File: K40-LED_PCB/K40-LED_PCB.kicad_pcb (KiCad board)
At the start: 2 copper layers, 41 x 27.8 mm, 14 parts, among them p1 12V_Pad

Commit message: Trace  deletion
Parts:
- D1, D10, D11, D12, D2, D3, D4, D5, D6, D7, D8, D9: footprint LRST-C190KGKT:LEDC1608X35N -> SPMWH1228FD5WATUS3_FOOTPRINT:LED_SPMWH1228FD5WARMSE
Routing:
- net Net-(D1-PadA): track 50.5 -> 0.00 mm
- net Net-(D10-PadC): track 33.1 -> 0.00 mm
- net Net-(R1-Pad1): track 7.19 -> 0.00 mm
- net Net-(D5-PadC): track 5.64 -> 0.00 mm
- net Net-(D3-PadC): track 5.64 -> 0.00 mm
- net Net-(D10-PadA): track 5.64 -> 0.00 mm
- net Net-(D11-PadA): track 5.62 -> 0.00 mm
- net Net-(D6-PadC): track 5.62 -> 0.00 mm
- net Net-(D1-PadC): track 5.62 -> 0.00 mm
- net Net-(D2-PadC): track 4.97 -> 0.00 mm
- net Net-(D12-PadA): track 4.89 -> 0.00 mm
- net Net-(D4-PadC): track 4.89 -> 0.00 mm

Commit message: More Footprint updates
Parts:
- R1: value 200 -> 18
- p1: footprint 12V_Pad:12V_Supply_Pad -> 12V_Through_Hole:12V_Through_Hole
- moved p1 15.7 mm to (92.0, 77.0), turned to 90 degrees
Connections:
- D10 pad A: Net-(D10-PadA) -> Net-(D1-PadA)
- D11 pad A: Net-(D11-PadA) -> Net-(D10-PadC)
- D11 pad C: Net-(D10-PadC) -> Net-(D11-PadC)
- D12 pad A: Net-(D12-PadA) -> Net-(D11-PadC)
- D12 pad C: Net-(D10-PadC) -> Net-(D12-PadC)
- D7 pad C: Net-(D10-PadA) -> Net-(D12-PadC)
- D8 pad C: Net-(D11-PadA) -> Net-(D12-PadC)
- D9 pad C: Net-(D12-PadA) -> Net-(D12-PadC)
- p1 pad 1: Net-(R1-Pad1) -> Net-(D12-PadC)
- p1 pad 2: Net-(D10-PadC) -> Net-(R1-Pad1)

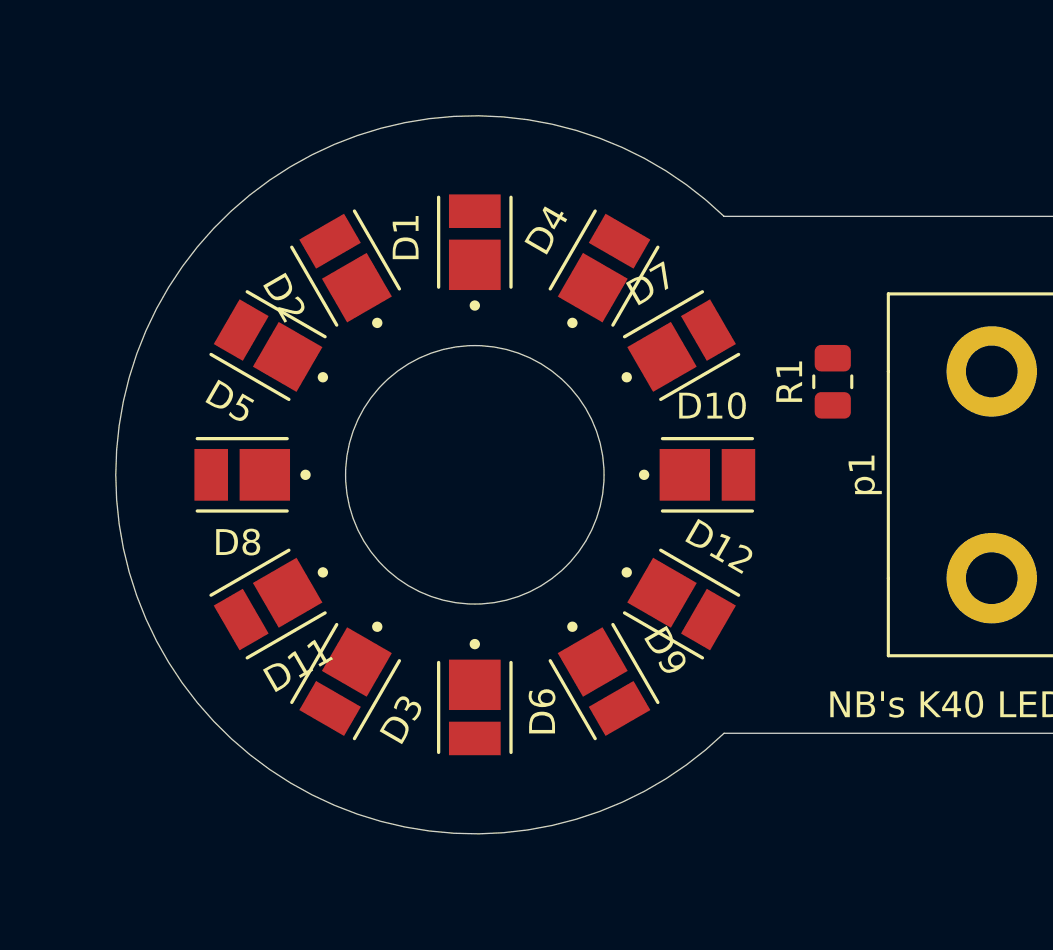
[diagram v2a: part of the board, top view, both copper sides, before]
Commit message: removed old footprint associations
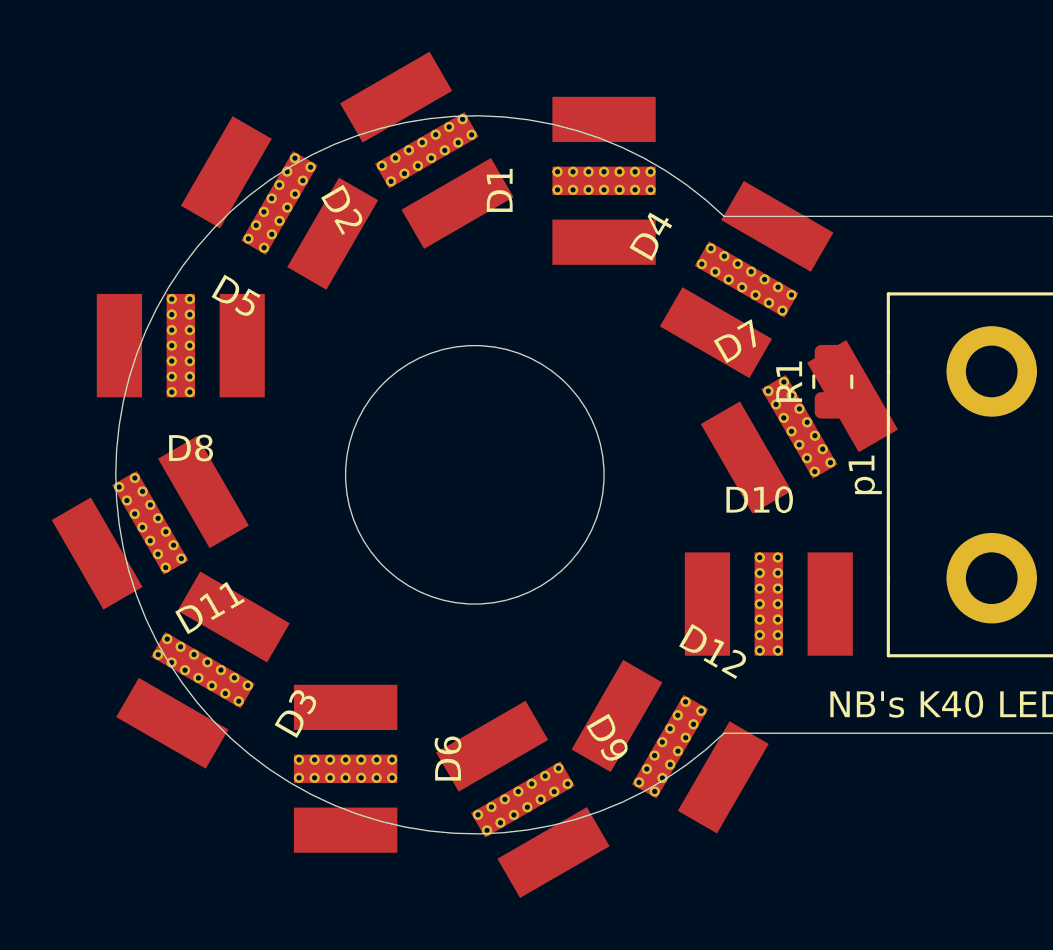
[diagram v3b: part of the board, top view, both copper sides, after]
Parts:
- D1, D10, D11, D12, D2, D3, D4, D5, D6, D7, D8, D9: footprint SPMWH1228FD5WATUS3_FOOTPRINT:LED_SPMWH1228FD5WARMSE -> Cree_MX3AWT-A1-R250-000BE3:Cree_MX3AWT-A1-R250-000BE3

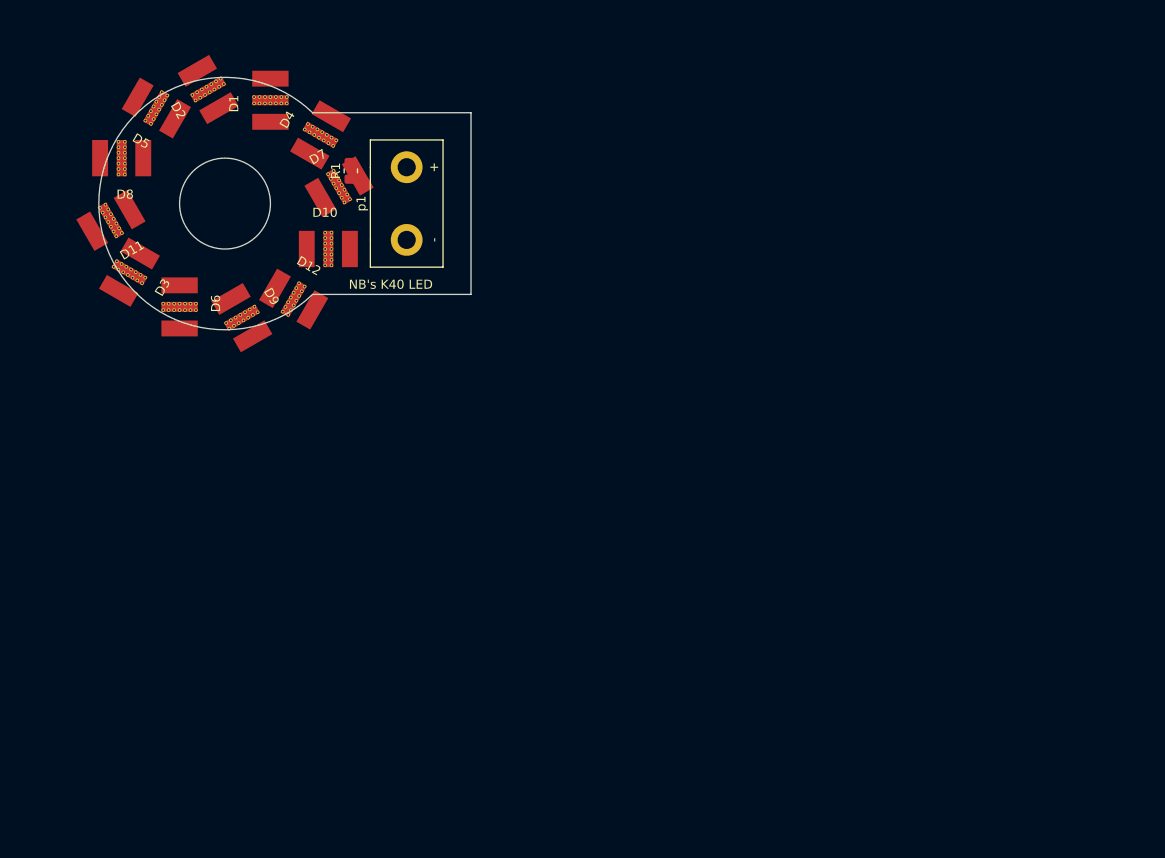
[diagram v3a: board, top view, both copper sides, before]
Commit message: PCB_Changes  + footprints
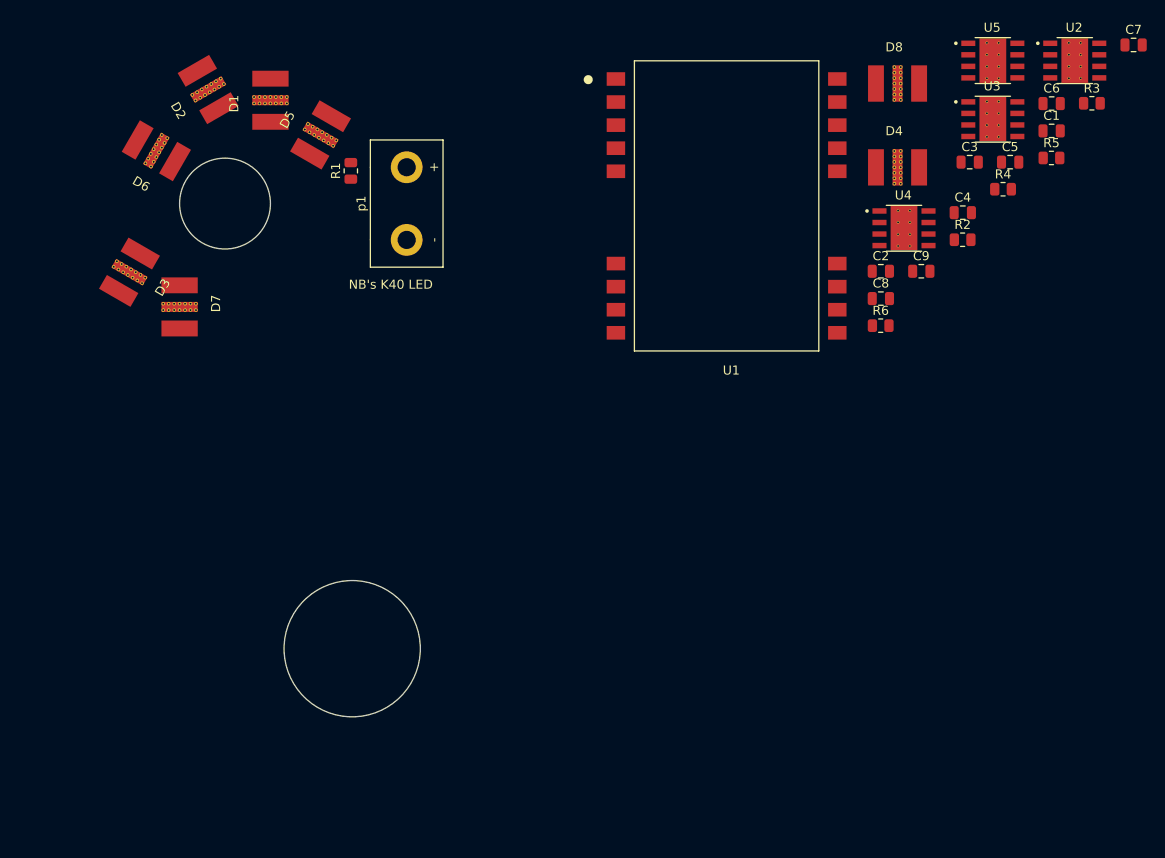
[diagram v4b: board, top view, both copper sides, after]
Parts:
- removed D10, D11, D12, D9: LTST-C190KGKT, Cree_MX3AWT-A1-R250-000BE3:Cree_MX3AWT-A1-R250-000BE3
- removed the D7 at (85.0, 68.0)
- added C1: 0.01uF, Capacitor_SMD:C_0805_2012Metric, F.Cu at (168.0, 65.0)
- added C2: 1uF, Capacitor_SMD:C_0805_2012Metric, F.Cu at (149.2, 80.5)
- added C3: 0.01uF, Capacitor_SMD:C_0805_2012Metric, F.Cu at (159.0, 68.4)
- added C4: 1uF, Capacitor_SMD:C_0805_2012Metric, F.Cu at (158.2, 74.0)
- added C5: 0.01uF, Capacitor_SMD:C_0805_2012Metric, F.Cu at (163.4, 68.4)
- added C6: 1uF, Capacitor_SMD:C_0805_2012Metric, F.Cu at (168.0, 62.0)
- added C7: 0.01uF, Capacitor_SMD:C_0805_2012Metric, F.Cu at (177.0, 55.5)
- added C8: 1uF, Capacitor_SMD:C_0805_2012Metric, F.Cu at (149.2, 83.5)
- added C9: 1uF, Capacitor_SMD:C_0805_2012Metric, F.Cu at (153.7, 80.5)
- added D4: LTST-C190KGKT, Cree_MX3AWT-A1-R250-000BE3:Cree_MX3AWT-A1-R250-000BE3, F.Cu at (148.7, 64.0)
- added R2: 1, Resistor_SMD:R_0805_2012Metric, F.Cu at (158.2, 77.0)
- added R3: 1, Resistor_SMD:R_0805_2012Metric, F.Cu at (172.4, 62.0)
- added R4: 1, Resistor_SMD:R_0805_2012Metric, F.Cu at (162.7, 71.4)
- added R5: 1, Resistor_SMD:R_0805_2012Metric, F.Cu at (168.0, 68.0)
- added R6: 51.1, Resistor_SMD:R_0805_2012Metric, F.Cu at (149.2, 86.4)
- added U1: LDD_350HS, LDD-350HS:LDD-350HS, F.Cu at (120.0, 54.8)
- added U2: LM3466, LM3466:NOPB, F.Cu at (170.5, 57.3)
- added U3: LM3466, LM3466:NOPB, F.Cu at (161.5, 63.7)
- added U4: LM3466, LM3466:NOPB, F.Cu at (151.7, 75.7)
- added U5: LM3466, LM3466:NOPB, F.Cu at (161.5, 57.3)
- R1: value 18 -> 13
- moved D8 82.7 mm to (148.7, 54.8), turned to 0 degrees
- moved D6 4.71 mm to (69.0, 72.7)
- renumbered D4 to D5, D5 to D6, D6 to D7
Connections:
- D1 pad A: Net-(D1-PadA) -> Net-(C1-Pad1)
- D2 pad A: Net-(D1-PadA) -> Net-(C1-Pad1)
- D3 pad A: Net-(D1-PadA) -> Net-(C1-Pad1)
- D6 pad C: Net-(D5-PadC) -> Net-(C4-Pad1)
- D8 pad A: Net-(D5-PadC) -> Net-(D4-PadC)
- D8 pad C: Net-(D12-PadC) -> Net-(C8-Pad1)
- R1 pad 2: Net-(D1-PadA) -> Net-(R1-Pad2)
- p1 pad 1: Net-(D12-PadC) -> Net-(p1-Pad1)
- p1 pad 2: Net-(R1-Pad1) -> Net-(p1-Pad2)
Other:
- board size 41 x 27.8 mm -> 26.5 x 61.5 mm

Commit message: PCB_Updates
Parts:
- moved D4 75.5 mm to (107.0, 127.0), turned to 180 degrees
- moved D8 71.8 mm to (106.9, 113.2), turned to 225 degrees
- moved D7 60.4 mm to (99.8, 137.9), turned to 135 degrees
- moved D3 58.7 mm to (85.9, 138.0), turned to 90 degrees
- moved D6 58.3 mm to (74.6, 130.7), turned to 45 degrees
- moved D2 52.0 mm to (74.6, 117.0), turned to 0 degrees
- moved D1 46.3 mm to (96.0, 106.2), turned to 270 degrees
- moved D5 41.7 mm to (82.2, 106.7), turned to 315 degrees

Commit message: PCB_Circular_Formation
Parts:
- moved D8 1.15 mm to (105.9, 113.7)
- moved D5 1.08 mm to (83.2, 107.1)
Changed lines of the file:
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@@
   )
   (module Cree_MX3AWT-A1-R250-000BE3:Cree_MX3AWT-A1-R250-000BE3 (layer F.Cu)
-    (at 106.894291 113.176777 225)
+    (at 105.894291 113.744134 225)
     (fp_text reference D8 (at 2 1 45) (layer F.SilkS)
       (effects (font (size 1 1) (thickness 0.15)))
@@
   )
   (module Cree_MX3AWT-A1-R250-000BE3:Cree_MX3AWT-A1-R250-000BE3 (layer F.Cu)
-    (at 82.176777 106.705127 315)
+    (at 83.176777 107.105709 315)
     (fp_text reference D5 (at 2 1 135) (layer F.SilkS)
       (effects (font (size 1 1) (thickness 0.15)))

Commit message: More circular changes correct
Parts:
- moved D6 1.73 mm to (76.1, 129.8)
- moved D7 1.41 mm to (98.8, 136.9)
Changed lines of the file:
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@@
   )
   (module Cree_MX3AWT-A1-R250-000BE3:Cree_MX3AWT-A1-R250-000BE3 (layer F.Cu)
-    (at 99.823223 137.894291 135)
+    (at 98.823223 136.894291 135)
     (fp_text reference D7 (at 2 1 135) (layer F.SilkS)
       (effects (font (size 1 1) (thickness 0.15)))
@@
   )
   (module Cree_MX3AWT-A1-R250-000BE3:Cree_MX3AWT-A1-R250-000BE3 (layer F.Cu)
-    (at 74.613621 130.705127 45)
+    (at 76.105709 129.823223 45)
     (fp_text reference D6 (at 2 1 45) (layer F.SilkS)
       (effects (font (size 1 1) (thickness 0.15)))

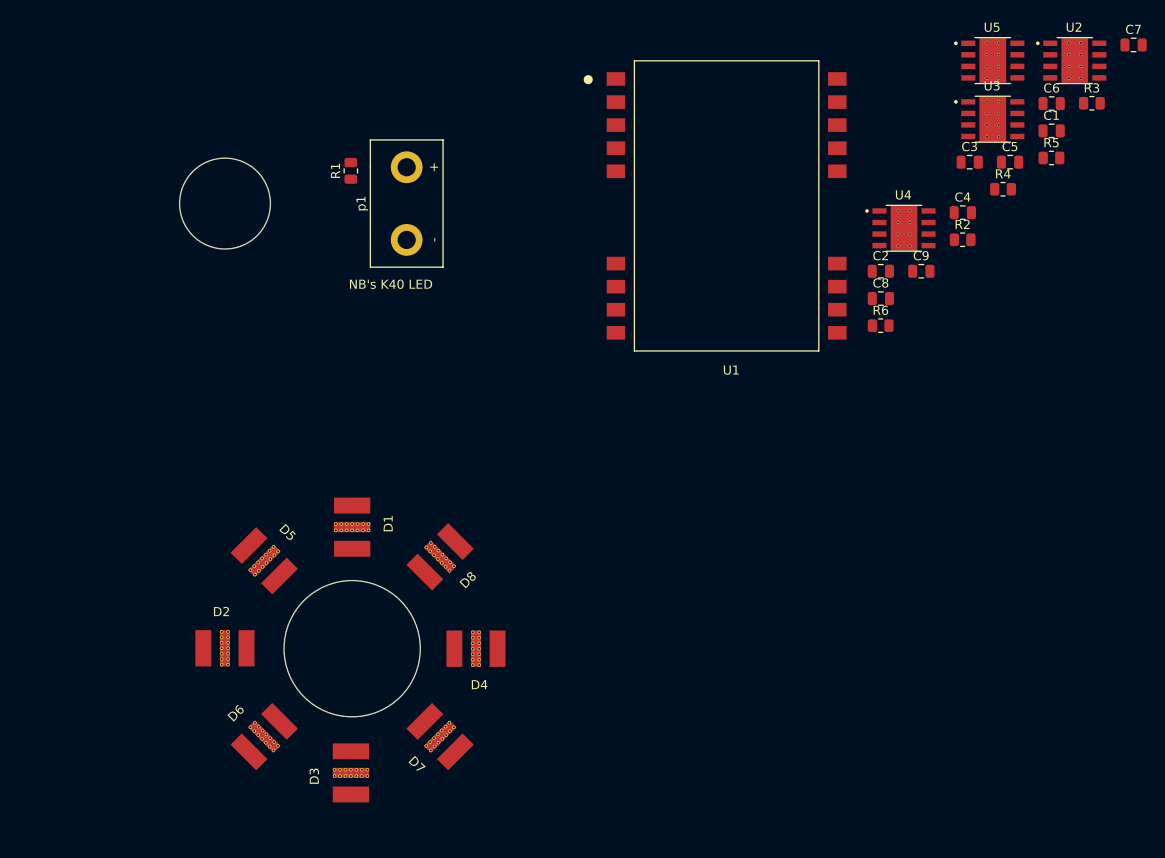
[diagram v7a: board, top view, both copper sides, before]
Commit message: PCB  Cathode traces
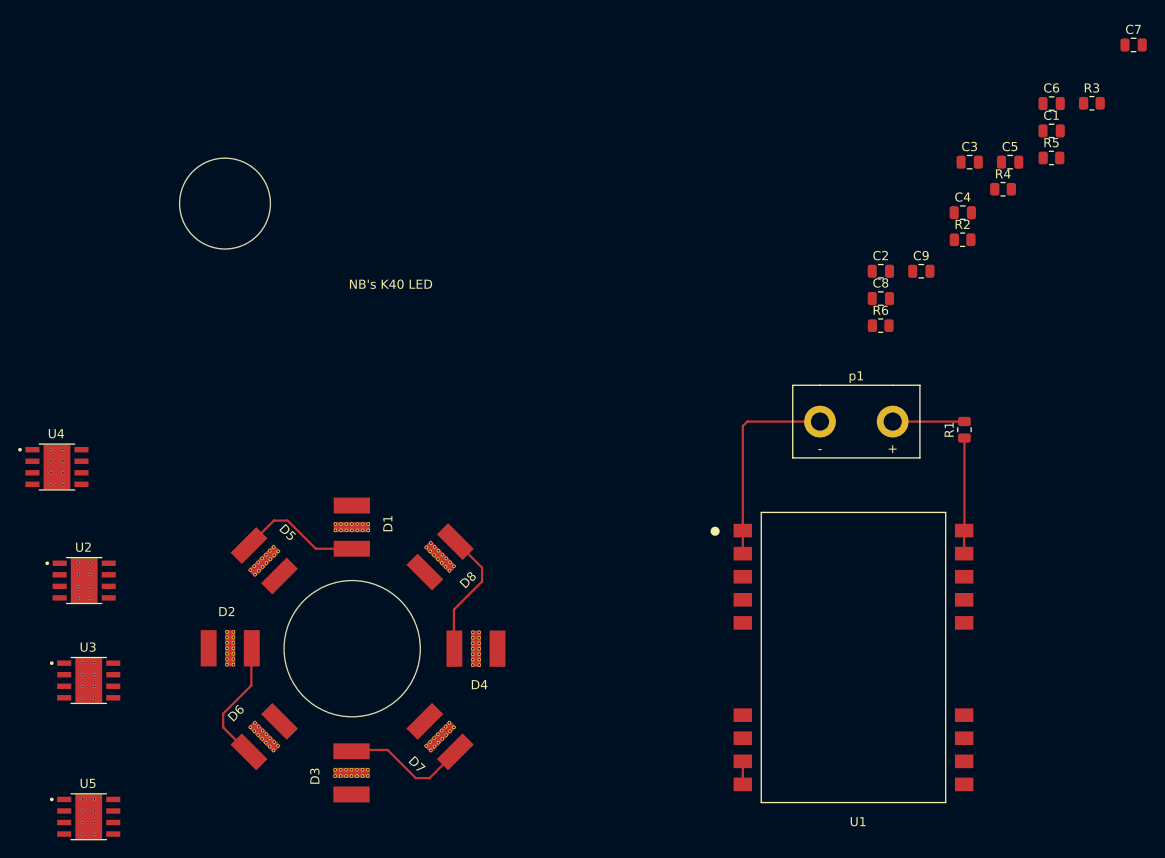
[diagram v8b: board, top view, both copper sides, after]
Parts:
- moved U5 129.7 mm to (62.0, 140.5)
- moved U2 123.2 mm to (61.5, 114.5)
- moved U3 117.1 mm to (62.0, 125.5)
- moved U4 96.9 mm to (58.5, 102.0)
- moved R1 73.3 mm to (158.4, 97.9)
- moved p1 52.7 mm to (142.5, 92.0), turned to 0 degrees
- moved U1 51.6 mm to (134.0, 104.5)
- moved D2 0.59 mm to (75.2, 117.0)
- moved D3 0.07 mm to (85.9, 138.0)
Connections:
- U1 pad 11: Net-(U1-Pad11) -> GND
- U1 pad 12: Net-(U1-Pad12) -> GND
- p1 pad 1: Net-(p1-Pad1) -> Net-(U1-Pad1)
- p1 pad 2: Net-(p1-Pad2) -> Net-(R1-Pad2)
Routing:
- net Net-(U1-Pad1): track 0.00 -> 22.7 mm
- net Net-(D2-PadC): track 0.00 -> 13.8 mm
- net Net-(D3-PadC): track 0.00 -> 13.8 mm
- net Net-(D1-PadC): track 0.00 -> 13.8 mm
- net Net-(D4-PadC): track 0.00 -> 13.8 mm
- net Net-(R1-Pad1): track 0.00 -> 12.7 mm
- net Net-(R1-Pad2): track 0.00 -> 7.91 mm
- net GND: track 0.00 -> 2.54 mm
